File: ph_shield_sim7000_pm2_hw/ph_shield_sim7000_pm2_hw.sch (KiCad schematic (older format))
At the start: 83 parts, among them J1 Conn_01x02, J2 Conn_01x05, J3 Conn_01x04, J4 USB_OTG, J5 I2C, J6 Conn_01x10, J7 SIM_Card, Q1 C1815, Q2 C1815, Q3 C1815, Q4 C1815, U1 TXS0108EPW, U2 LM2596S-ADJ, U3 SIM7000E, U4 TVS_Diode_Array_SMF05C

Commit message: Darwing Layout SIM7000
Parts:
- removed J2: Conn_01x05, Connector_PinHeader_2.54mm:PinHeader_1x05_P2.54mm_Vertical, symbol Connector_Generic:Conn_01x05
- added J2: Conn_01x07, Connector_PinHeader_2.54mm:PinHeader_1x07_P2.54mm_Vertical, symbol Connector_Generic:Conn_01x07
- AE1, AE3: footprint (none) -> VinhTho_Lib:Anten_GSM_IPEX
- AE2, AE4: footprint VinhTho_Lib:MOLEX_0731000114 -> VinhTho_Lib:Anten_GPS
- C14: value 33p -> 33pF
- C18, C19, C20: value 100uF/25V -> 100uF/16V; footprint Capacitors_SMD:CP_Elec_10x10 -> Capacitor_Tantalum_SMD:CP_EIA-6032-28_Kemet-C_Pad2.25x2.35mm_HandSolder
- C7: value 330uF/25V -> 330uF/10V; footprint Capacitors_SMD:CP_Elec_10x10 -> Capacitor_Tantalum_SMD:CP_EIA-7343-30_AVX-N_Pad2.25x2.55mm_HandSolder
- J7: footprint (none) -> VinhTho_Lib:socket_sim_6p
- R1, R10, R11, R12, R16, R17, R18, R19, R2, R20, R21, R22, R23, R24, R3, R4, R5, R6, R7, R8, R9: footprint Resistors_SMD:R_0805_HandSoldering -> Resistor_SMD:R_0603_1608Metric_Pad1.05x0.95mm_HandSolder
- R14, R15: value R -> 0R
- U2: footprint TO-263-5 -> Package_TO_SOT_SMD:TO-263-5_TabPin3
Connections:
- wire segments 305 -> 307

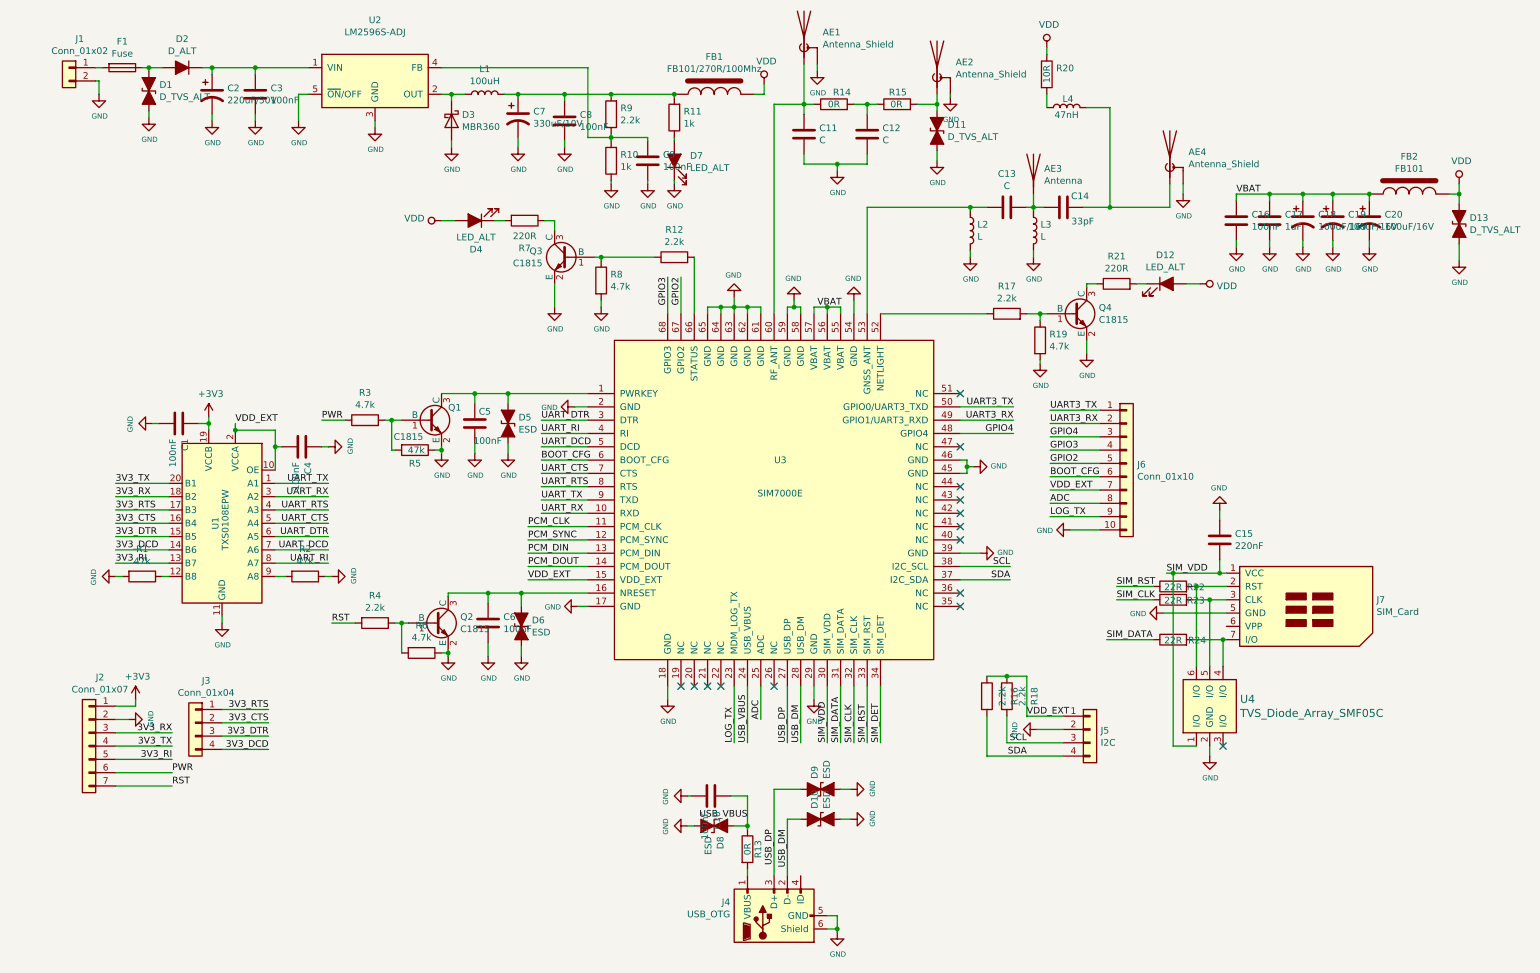
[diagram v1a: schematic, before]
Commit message: Design Schematic SIM7000E
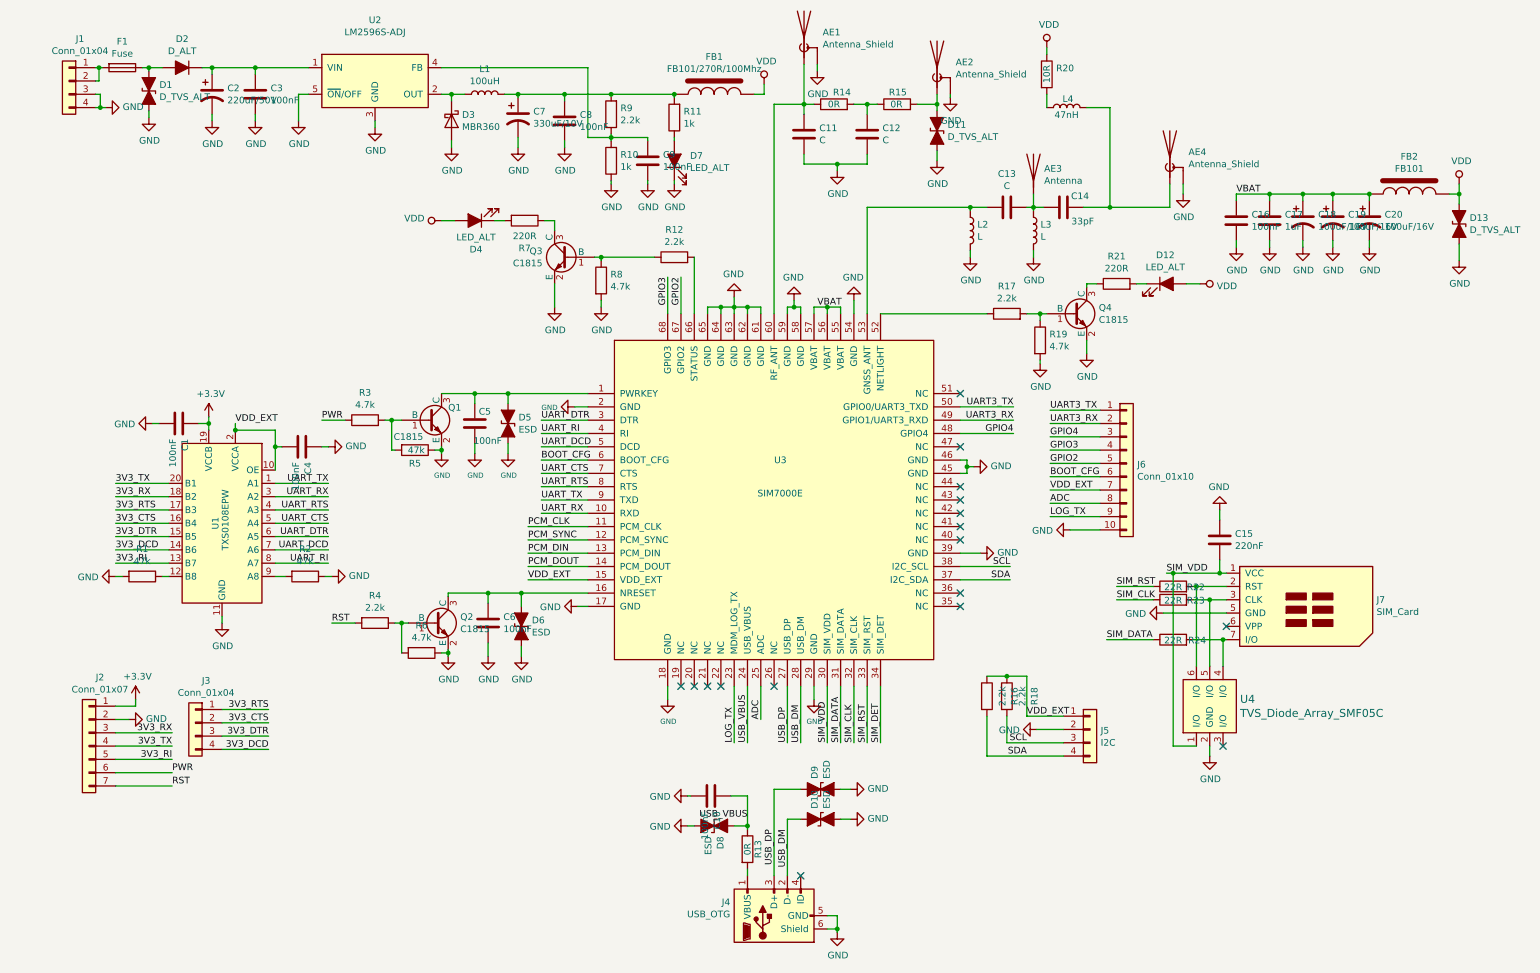
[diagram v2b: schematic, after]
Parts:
- removed J1: Conn_01x02, VinhTho_Lib:TerminalBlock_WAGO-236_2Stift_R5mm_2pol, symbol Connector_Generic:Conn_01x02
- added J1: Conn_01x04, VinhTho_Lib:Header-4pin-2.54, symbol Connector_Generic:Conn_01x04
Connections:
- net GND: now reaches J5.2 (Pin_2)
- net GND: now also AE1.2 (Shield), AE2.2 (Shield), AE4.2 (Shield), C1.2, C10.1, C11.2, C12.2, C15.2, C16.2, C17.2, C18.2, C19.2, C2.2, C20.2, C3.2, C4.1, C6.2, C7.2, C8.2, C9.2, D1.2 (A2), D10.2 (A2), D11.2 (A2), D13.2 (A2), D3.2 (A), D6.2 (A2), D7.1 (K), D8.2 (A2), D9.2 (A2), J2.2 (Pin_2), J4.5 (GND), J4.6 (Shield), J6.10 (Pin_10), J7.5 (GND), L2.2, L3.2, Q2.2 (E), Q3.2 (E), Q4.2 (E), R1.2, R10.1, R19.2, R2.1, R6.1, R8.2, U1.11 (GND), U2.3 (GND), U2.5 (~ON~/OFF), U3.17 (GND), U3.39 (GND), U3.45 (GND), U3.46 (GND), U3.54 (GND), U3.58 (GND), U3.59 (GND), U3.61 (GND), U3.62 (GND), U3.63 (GND), U3.64 (GND), U3.65 (GND), U4.2 (GND), J1.3 (Pin_3), J1.4 (Pin_4)
- net at F1.2: now also J1.1 (Pin_1), J1.2 (Pin_2)
- net +3V3: now reaches J2.1 (Pin_1)
- net +3V3: now also C1.1, U1.19 (VCCB)
- no-connect marks 15 -> 17
